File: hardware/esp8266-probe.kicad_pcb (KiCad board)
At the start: 2 copper layers, 50 x 38 mm, 31 parts, among them J1 USB_C_Receptacle_USB2.0, J2 Debug, J3 Target, SW1 Reset, SW2 Flash, U1 LD1117DT33, U2 ESP-12E

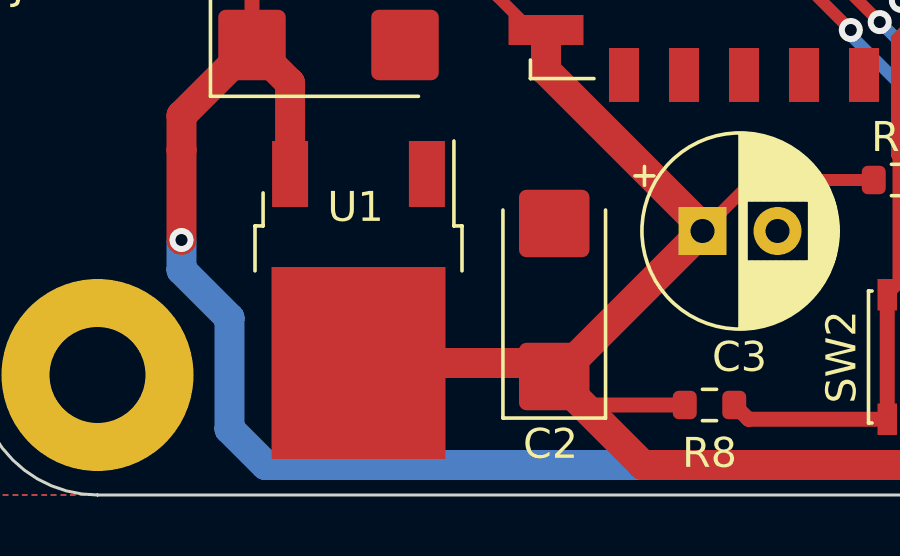
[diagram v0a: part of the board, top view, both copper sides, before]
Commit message: Improve thermal design around the linear regulator.
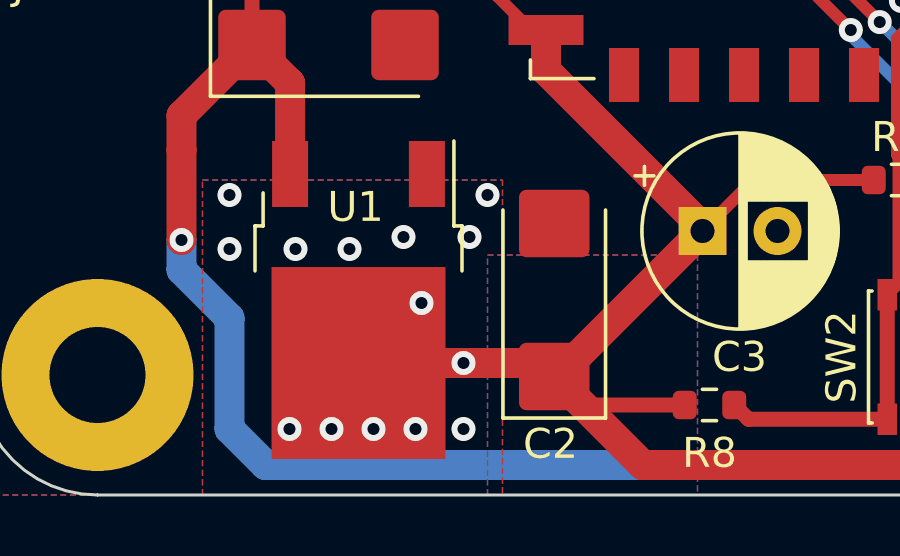
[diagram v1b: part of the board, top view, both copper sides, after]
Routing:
- net +3V3: vias 0 -> 14
- added copper zone on B.Cu, net +3V3
- added copper zone on F.Cu, net +3V3
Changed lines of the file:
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@@
   (segment (start 118.617621 94.05) (end 123.467621 89.2) (width 1) (layer "F.Cu") (net 3))
   (segment (start 114.29952 75.25) (end 116.600489 77.550969) (width 0.4) (layer "F.Cu") (net 3))
-  (segment (start 112 93.6) (end 118.075 93.6) (width 1) (layer "F.Cu") (net 3))
+  (segment (start 112 93.6) (end 115.5 93.6) (width 1) (layer "F.Cu") (net 3))
+  (segment (start 115.5 93.6) (end 118.075 93.6) (width 1) (layer "F.Cu") (net 3))
   (segment (start 125.167621 87.5) (end 123.467621 89.2) (width 0.4) (layer "F.Cu") (net 3))
+  (via (at 109.9 89.8) (size 0.8) (drill 0.4) (layers "F.Cu" "B.Cu") (free) (net 3))
+  (via (at 114.1 91.6) (size 0.8) (drill 0.4) (layers "F.Cu" "B.Cu") (net 3))
+  (via (at 116.3 88) (size 0.8) (drill 0.4) (layers "F.Cu" "B.Cu") (free) (net 3))
+  (via (at 113.9 95.8) (size 0.8) (drill 0.4) (layers "F.Cu" "B.Cu") (net 3))
+  (via (at 111.7 89.8) (size 0.8) (drill 0.4) (layers "F.Cu" "B.Cu") (free) (net 3))
+  (via (at 115.5 95.8) (size 0.8) (drill 0.4) (layers "F.Cu" "B.Cu") (free) (net 3))
+  (via (at 107.7 88) (size 0.8) (drill 0.4) (layers "F.Cu" "B.Cu") (free) (net 3))
+  (via (at 115.7 89.4) (size 0.8) (drill 0.4) (layers "F.Cu" "B.Cu") (free) (net 3))
+  (via (at 115.5 93.6) (size 0.8) (drill 0.4) (layers "F.Cu" "B.Cu") (net 3))
+  (via (at 111.1 95.8) (size 0.8) (drill 0.4) (layers "F.Cu" "B.Cu") (net 3))
+  (via (at 107.7 89.8) (size 0.8) (drill 0.4) (layers "F.Cu" "B.Cu") (free) (net 3))
+  (via (at 112.5 95.8) (size 0.8) (drill 0.4) (layers "F.Cu" "B.Cu") (net 3))
+  (via (at 113.5 89.4) (size 0.8) (drill 0.4) (layers "F.Cu" "B.Cu") (free) (net 3))
+  (via (at 109.7 95.8) (size 0.8) (drill 0.4) (layers "F.Cu" "B.Cu") (net 3))
   (segment (start 107.27 73.499022) (end 107.27 72.055) (width 0.3) (layer "F.Cu") (net 4))
   (segment (start 107.019022 73.75) (end 107.27 73.499022) (width 0.3) (layer "F.Cu") (net 4))
@@
       )
     )
+  )
+  (zone (net 3) (net_name "+3V3") (layers F&B.Cu) (hatch edge 0.508)
+    (priority 1)
+    (connect_pads (clearance 0.508))
+    (min_thickness 0.254) (filled_areas_thickness no)
+    (fill yes (thermal_gap 0.508) (thermal_bridge_width 0.508))
+    (polygon
+      (pts
+        (xy 123.3 98)
+        (xy 116.3 98)
+        (xy 116.3 90)
+        (xy 123.3 90)
+      )
+    )
+  )
+  (zone (net 3) (net_name "+3V3") (layers F&B.Cu) (hatch edge 0.508)
+    (priority 1)
+    (connect_pads yes (clearance 0.508))
+    (min_thickness 0.254) (filled_areas_thickness no)
+    (fill yes (thermal_gap 0.508) (thermal_bridge_width 0.508))
+    (polygon
+      (pts
+        (xy 116.8 98)
+        (xy 106.8 98)
+        (xy 106.8 87.5)
+        (xy 116.8 87.5)
+      )
+    )

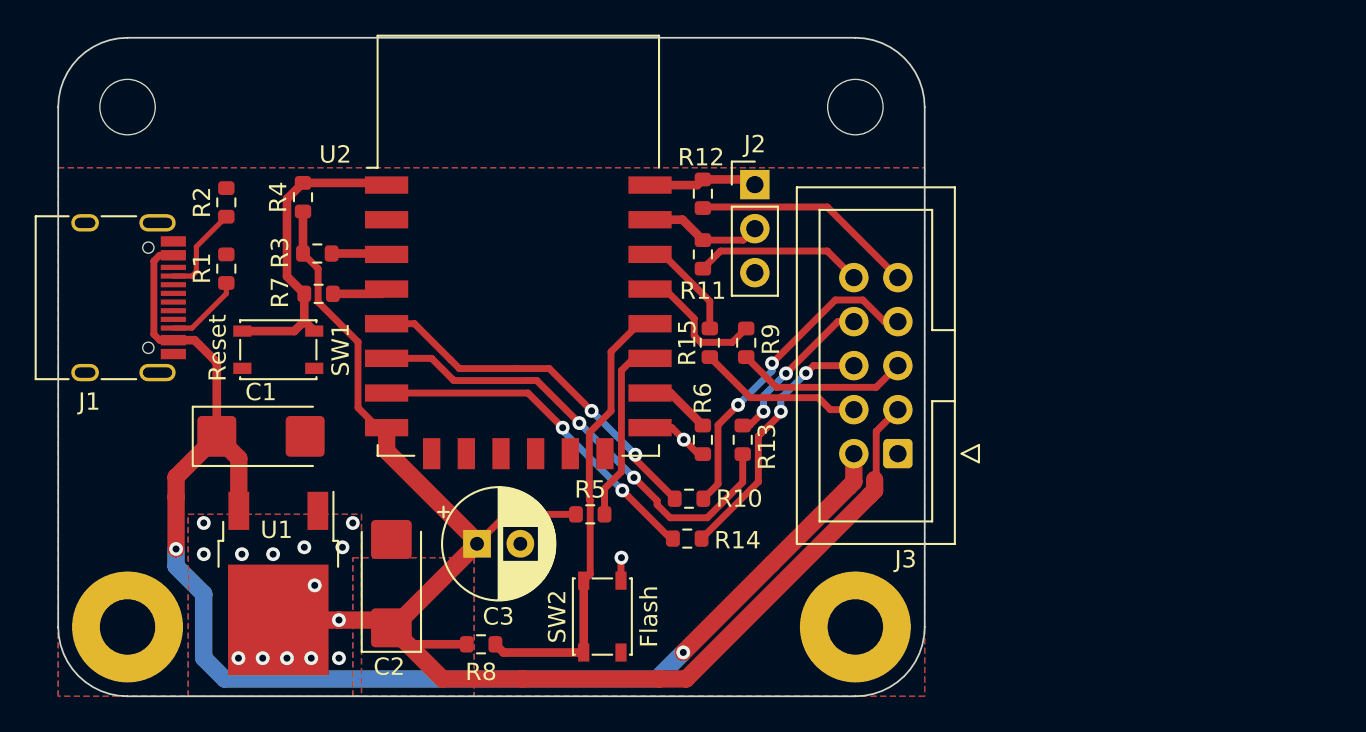
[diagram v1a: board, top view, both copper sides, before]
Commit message: Add more ground vias.
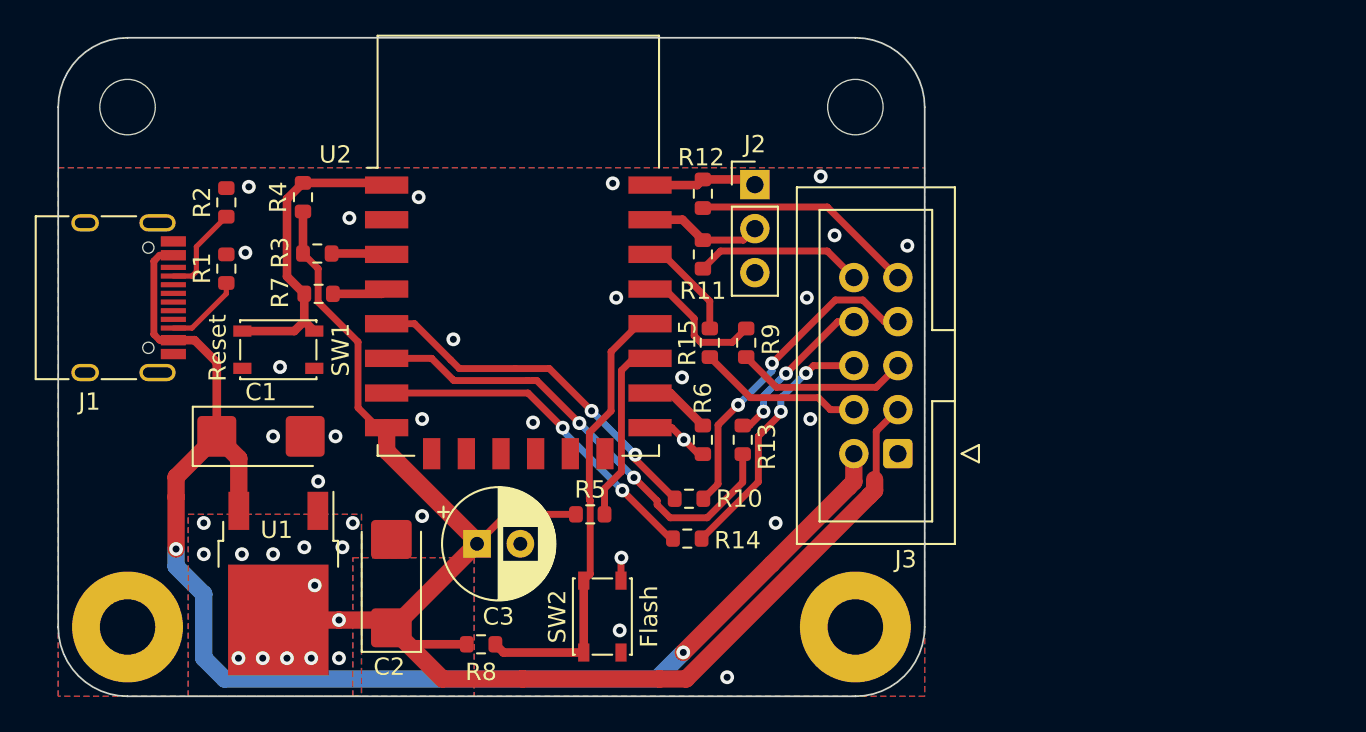
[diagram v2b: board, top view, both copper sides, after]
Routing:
- net GND: vias 2 -> 25
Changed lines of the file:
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@@
   (segment (start 134.71 82.5) (end 135.4 83.19) (width 0.4) (layer "F.Cu") (net 2))
   (segment (start 133.45 82.5) (end 134.71 82.5) (width 0.4) (layer "F.Cu") (net 2))
+  (via (at 140.7 88) (size 0.8) (drill 0.4) (layers "F.Cu" "B.Cu") (free) (net 2))
   (via (at 135.4 83.19) (size 0.8) (drill 0.4) (layers "F.Cu" "B.Cu") (net 2))
+  (via (at 110.1 72.4) (size 0.8) (drill 0.4) (layers "F.Cu" "B.Cu") (free) (net 2))
+  (via (at 112.1 79) (size 0.8) (drill 0.4) (layers "F.Cu" "B.Cu") (free) (net 2))
+  (via (at 144.1 71.4) (size 0.8) (drill 0.4) (layers "F.Cu" "B.Cu") (free) (net 2))
+  (via (at 111.7 83) (size 0.8) (drill 0.4) (layers "F.Cu" "B.Cu") (free) (net 2))
+  (via (at 131.5 75) (size 0.8) (drill 0.4) (layers "F.Cu" "B.Cu") (free) (net 2))
+  (via (at 131.7 94.2) (size 0.8) (drill 0.4) (layers "F.Cu" "B.Cu") (free) (net 2))
+  (via (at 120.3 87.6) (size 0.8) (drill 0.4) (layers "F.Cu" "B.Cu") (free) (net 2))
+  (via (at 137.9 96.9) (size 0.8) (drill 0.4) (layers "F.Cu" "B.Cu") (free) (net 2))
+  (via (at 110.3 68.6) (size 0.8) (drill 0.4) (layers "F.Cu" "B.Cu") (free) (net 2))
+  (via (at 148.3 72) (size 0.8) (drill 0.4) (layers "F.Cu" "B.Cu") (free) (net 2))
+  (via (at 115.3 83) (size 0.8) (drill 0.4) (layers "F.Cu" "B.Cu") (free) (net 2))
+  (via (at 122.1 77.4) (size 0.8) (drill 0.4) (layers "F.Cu" "B.Cu") (free) (net 2))
   (via (at 131.8 90) (size 0.8) (drill 0.4) (layers "F.Cu" "B.Cu") (net 2))
+  (via (at 120.3 82) (size 0.8) (drill 0.4) (layers "F.Cu" "B.Cu") (free) (net 2))
+  (via (at 142.7 82) (size 0.8) (drill 0.4) (layers "F.Cu" "B.Cu") (free) (net 2))
+  (via (at 116.1 70.4) (size 0.8) (drill 0.4) (layers "F.Cu" "B.Cu") (free) (net 2))
+  (via (at 135.3 79.6) (size 0.8) (drill 0.4) (layers "F.Cu" "B.Cu") (free) (net 2))
+  (via (at 143.3 68) (size 0.8) (drill 0.4) (layers "F.Cu" "B.Cu") (free) (net 2))
+  (via (at 126.7 82.2) (size 0.8) (drill 0.4) (layers "F.Cu" "B.Cu") (free) (net 2))
+  (via (at 114.3 85.6) (size 0.8) (drill 0.4) (layers "F.Cu" "B.Cu") (free) (net 2))
+  (via (at 120.1 69.2) (size 0.8) (drill 0.4) (layers "F.Cu" "B.Cu") (free) (net 2))
+  (via (at 131.3 68.4) (size 0.8) (drill 0.4) (layers "F.Cu" "B.Cu") (free) (net 2))
+  (via (at 142.5 75) (size 0.8) (drill 0.4) (layers "F.Cu" "B.Cu") (free) (net 2))
   (segment (start 146.123189 86.413188) (end 146.41202 86.124357) (width 1) (layer "F.Cu") (net 3))
   (segment (start 126.1 97) (end 134 97) (width 1) (layer "F.Cu") (net 3))

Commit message: Added level shifters and power to the PCB.
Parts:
- added C10: 0.1uF, Capacitor_SMD:C_0603_1608Metric, F.Cu at (153.4, 68.7)
- added C11: 0.1uF, Capacitor_SMD:C_0603_1608Metric, F.Cu at (150.0, 75.0)
- added C4: 0.1uF, Capacitor_SMD:C_0603_1608Metric, F.Cu at (141.3, 73.9)
- added C5: 0.1uF, Capacitor_SMD:C_0603_1608Metric, F.Cu at (144.6, 86.7)
- added C6: 0.1uF, Capacitor_SMD:C_0603_1608Metric, F.Cu at (146.0, 68.6)
- added C7: 0.1uF, Capacitor_SMD:C_0603_1608Metric, F.Cu at (144.5, 80.2)
- added C8: 0.1uF, Capacitor_SMD:C_0603_1608Metric, F.Cu at (148.6, 86.7)
- added C9: 0.1uF, Capacitor_SMD:C_0603_1608Metric, F.Cu at (154.0, 78.2)
- added Q1: BC817, Package_TO_SOT_SMD:SOT-23, F.Cu at (145.1, 94.4)
- added Q2: NX2301P, Package_TO_SOT_SMD:SOT-23, F.Cu at (135.4, 94.5)
- added Q3: BC817, Package_TO_SOT_SMD:SOT-23, F.Cu at (135.4, 89.6)
- added Q4: NX2301P, Package_TO_SOT_SMD:SOT-23, F.Cu at (140.1, 94.4)
- added R16: 100, Resistor_SMD:R_0603_1608Metric, F.Cu at (149.4, 95.4)
- added R17: DNP, Resistor_SMD:R_0603_1608Metric, F.Cu at (149.7, 68.6)
- added R18: DNP, Resistor_SMD:R_0603_1608Metric, F.Cu at (138.8, 78.7)
- added R19: DNP, Resistor_SMD:R_0603_1608Metric, F.Cu at (144.4, 72.5)
- added R20: DNP, Resistor_SMD:R_0603_1608Metric, F.Cu at (150.2, 84.4)
- added R21: DNP, Resistor_SMD:R_0603_1608Metric, F.Cu at (150.2, 78.2)
- added R22: 10K, Resistor_SMD:R_0603_1608Metric, F.Cu at (141.3, 86.6)
- added R23: DNP, Resistor_SMD:R_0603_1608Metric, F.Cu at (143.7, 83.4)
- added R24: 10K, Resistor_SMD:R_0603_1608Metric, F.Cu at (151.3, 91.5)
- added R25: 100, Resistor_SMD:R_0603_1608Metric, F.Cu at (138.8, 76.6)
- added R26: 12K, Resistor_SMD:R_0603_1608Metric, F.Cu at (142.8, 68.8)
- added R27: 47K, Resistor_SMD:R_0603_1608Metric, F.Cu at (140.6, 68.8)
- added R28: 100, Resistor_SMD:R_0603_1608Metric, F.Cu at (141.3, 71.7)
- added R29: 100, Resistor_SMD:R_0603_1608Metric, F.Cu at (140.9, 82.8)
- added R30: 10K, Resistor_SMD:R_0603_1608Metric, F.Cu at (138.7, 83.2)
- added R31: 100K, Resistor_SMD:R_0603_1608Metric, F.Cu at (139.7, 91.0)
- added U3: 74LVC2T45DCT, Package_SO:VSSOP-8_3.0x3.0mm_P0.65mm, F.Cu at (149.7, 71.9)
- added U4: 74LVC2T45DCT, Package_SO:VSSOP-8_3.0x3.0mm_P0.65mm, F.Cu at (144.5, 77.0)
- added U5: 74LVC2T45DCT, Package_SO:VSSOP-8_3.0x3.0mm_P0.65mm, F.Cu at (150.2, 81.5)
- added U6: 74LVC2T45DCT, Package_SO:VSSOP-8_3.0x3.0mm_P0.65mm, F.Cu at (146.6, 89.9)
- R13: value 100 -> 1K
- moved R10 25.5 mm to (157.8, 73.8)
- moved R14 24.4 mm to (157.9, 79.1)
- moved R11 21.6 mm to (157.8, 76.1), turned to 0 degrees
- moved R15 21.4 mm to (157.9, 81.5), turned to 0 degrees
- moved J3 20.3 mm to (168.1, 84.0)
- moved H2 20.0 mm to (165.3, 94.0)
- moved H3 20.0 mm to (165.3, 64.0)
- moved R9 20.0 mm to (157.9, 84.0), turned to 0 degrees
- moved R12 19.0 mm to (155.4, 70.8), turned to 0 degrees
- moved R13 3.70 mm to (136.7, 86.2), turned to 0 degrees
- moved J2 2.00 mm to (137.5, 68.5)
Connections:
- net Net-(R5-Pad2) renamed /SWDIO_DIR
- net Net-(R6-Pad1) renamed /POWER
- J2 pad 1: Net-(J2-Pad1) -> /TX_HOST
- J2 pad 2: Net-(J2-Pad2) -> /RX_HOST
- J3 pad 2: +5V -> +3V3
- J3 pad 3: +3V3 -> /VREF
- R10 pad 2: /TDO -> /RX
- R11 pad 1: Net-(J2-Pad2) -> Net-(R11-Pad1)
- R11 pad 2: /RX -> /TDO
- R12 pad 1: Net-(J2-Pad1) -> Net-(R12-Pad1)
- R13 pad 2: /SRST -> Net-(Q1-Pad1)
- R9 pad 1: Net-(R9-Pad1) -> Net-(R23-Pad2)
- U2 pad 19: Net-(R9-Pad1) -> /TMS_SWDIO_HOST
- U2 pad 2: unconnected-(U2-Pad2) -> Net-(R26-Pad1)
- U2 pad 20: Net-(R15-Pad1) -> /TCK_SWCLK_HOST
- U2 pad 21: Net-(J2-Pad2) -> /RX_HOST
- U2 pad 22: Net-(J2-Pad1) -> /TX_HOST
- U2 pad 5: Net-(R10-Pad1) -> /TDO_HOST
- U2 pad 7: Net-(R14-Pad1) -> /TDI_HOST
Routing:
- net /VREF: track 0.00 -> 107.3 mm, vias 0 -> 2
- net +3V3: track 87.3 -> 178.0 mm, vias 14 -> 27
- net +5V: track 77.7 -> 18.9 mm, vias 2 -> 0
- net /TDI_HOST: track 0.00 -> 44.4 mm, vias 0 -> 2
- net /TDO_HOST: track 0.00 -> 27.3 mm
- net /TCK_SWCLK_HOST: track 0.00 -> 25.2 mm
- net /SWDIO_DIR: track 10.6 -> 35.7 mm
- net Net-(R26-Pad1): track 0.00 -> 24.9 mm
- net GND: track 5.02 -> 25.1 mm, vias 25 -> 54
- net Net-(R23-Pad2): track 0.00 -> 19.2 mm
- net /SRST: track 9.42 -> 28.5 mm, vias 2 -> 0
- net /TX_HOST: track 0.00 -> 19.1 mm
- net Net-(R11-Pad1): track 0.00 -> 18.9 mm
- net /TMS_SWDIO_HOST: track 0.00 -> 16.5 mm
- net /RX_HOST: track 0.00 -> 12.2 mm
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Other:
- board size 50 x 38 mm -> 70 x 38 mm
